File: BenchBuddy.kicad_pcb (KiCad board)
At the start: 4 copper layers, 165.1 x 63.5 mm, 133 parts, among them K1 1461069-5, P1 24 Pin MiniFit JR, P2 CONN_3X2, P3 CONN_2, P4 12 Pin Terminal Block, P5 3 Pin TB, Q1 2N3904, Q2 DMN65D8L-7, Q3 AOD476, Q4 AOD476, SW1 Power Switch, U1 LTV-816S, U11 LM317, U2 MCP3901, U3 LMT84, U4 OPA4170, U5 MCP4801, U6 LM337T, U7 AP5726, U8 LM337T, U9 LM317

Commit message: Layout Work Session 8 Output
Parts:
- R2, R5: moved to F.Cu
- moved R43 48.7 mm to (143.0, 99.8), turned to 90 degrees
- moved R1 16.1 mm to (159.3, 137.7), turned to 0 degrees
- moved R2 10.7 mm to (174.5, 126.0), turned to 0 degrees
- moved R26 7.13 mm to (120.1, 132.0)
- moved R27 7.13 mm to (122.7, 132.0)
- moved R28 7.13 mm to (125.1, 132.0)
- moved R29 7.13 mm to (128.0, 131.7)
- moved R31 6.35 mm to (135.5, 132.0)
- moved R30 6.35 mm to (132.6, 131.9)
- moved R32 6.35 mm to (137.9, 132.1)
- moved D1 5.99 mm to (172.2, 130.6), turned to 90 degrees
- moved R4 5.19 mm to (180.3, 137.9), turned to 0 degrees
- moved R3 5.06 mm to (178.8, 129.0), turned to 180 degrees
- moved R40 4.65 mm to (128.0, 94.5)
- moved R51 3.62 mm to (140.7, 94.5)
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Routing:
- net /Arduino/RELAY+: track 0.00 -> 54.5 mm
- net /Arduino/RELAY-: track 0.00 -> 44.3 mm
- net N-0000090: track 0.00 -> 20.1 mm
- net N-0000089: track 0.00 -> 19.2 mm
- net N-0000088: track 0.00 -> 13.9 mm, vias 0 -> 1
- net N-0000086: track 0.00 -> 13.7 mm
- net +12P: track 48.7 -> 62.0 mm, vias 2 -> 3
- net N-0000091: track 0.00 -> 8.35 mm
- net N-0000092: track 0.00 -> 5.56 mm, vias 0 -> 1
- net N-0000056: track 0.00 -> 5.18 mm
- net N-0000084: track 0.00 -> 4.38 mm
- net GND: track 30.6 -> 33.9 mm
- net GND_RELAY: track 1.65 -> 3.77 mm

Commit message: Layout Work Session 9 Output
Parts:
- moved C22 9.63 mm to (176.0, 90.4), turned to 270 degrees
- moved C17 7.56 mm to (178.1, 90.4), turned to 270 degrees
- moved D10 7.08 mm to (195.1, 90.7)
- moved C16 5.65 mm to (155.7, 89.9), turned to 270 degrees
- moved D8 5.50 mm to (174.5, 83.1), turned to 270 degrees
- moved D3 2.22 mm to (154.2, 83.1)
- moved R21 2.10 mm to (140.5, 78.7)
- moved C19 1.76 mm to (174.0, 90.4), turned to 270 degrees
- moved C20 1.67 mm to (196.6, 86.4)
- moved D9 1.67 mm to (185.9, 85.6)
- moved C18 1.65 mm to (159.8, 89.9), turned to 270 degrees
- moved C21 1.48 mm to (199.9, 85.6), turned to 0 degrees
- moved R53 0.90 mm to (203.7, 85.6)
- moved C23 0.86 mm to (157.7, 89.9), turned to 270 degrees
- moved D6 0.80 mm to (179.1, 82.8)
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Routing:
- net /PowerAdjustmentMonitor/V+_ADJ: track 0.00 -> 92.2 mm
- net /PowerAdjustmentMonitor/V-_ADJ: track 0.00 -> 89.7 mm
- net N-00000124: track 0.00 -> 57.0 mm
- net N-00000125: track 0.00 -> 48.0 mm
- net GND_PWR: track 0.00 -> 22.6 mm, vias 0 -> 1
- net +12V: track 209.0 -> 215.1 mm
- net +3.3V: track 145.5 -> 151.5 mm, vias 0 -> 1
- net -12V: track 212.4 -> 213.5 mm
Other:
- board text added: "ADD OUTPUT CAPACITANCE?"

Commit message: Layout Work Session 10 Output
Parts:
- C6: moved to F.Cu
- moved C6 38.4 mm to (208.0, 119.9), turned to 0 degrees
- moved C5 12.9 mm to (154.2, 120.7)
- moved R17 11.9 mm to (161.3, 115.6), turned to 180 degrees
- moved U7 10.5 mm to (159.3, 118.6), turned to 90 degrees
- moved C12 9.39 mm to (158.2, 108.7)
- moved L4 6.99 mm to (167.9, 120.7), turned to 90 degrees
- moved D5 6.80 mm to (172.2, 120.4), turned to 270 degrees
- moved JP4 0.57 mm to (89.7, 121.9)
- moved JP3 0.51 mm to (95.5, 117.3)
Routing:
- net +5P: track 10.5 -> 216.9 mm, vias 2 -> 3
- net /LED_Driver/LED_STRING+: track 0.00 -> 66.9 mm, vias 0 -> 2
- net /LED_Driver/LED_STRING-: track 0.00 -> 60.3 mm, vias 0 -> 2
- net N-00000120: track 0.00 -> 14.2 mm
- net GND_LED: track 2.83 -> 7.56 mm, vias 1 -> 4

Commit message: Layout Work Session 11 Output
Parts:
- added L5: INDUCTOR, SM0805, B.Cu at (165.2, 99.9)
- C6, R11: moved to B.Cu
- R16, R48, R49: moved to F.Cu
- moved C7 58.1 mm to (168.9, 99.9), turned to 180 degrees
- moved C1 53.0 mm to (167.5, 94.9), turned to 180 degrees
- moved C8 48.7 mm to (161.5, 99.9), turned to 180 degrees
- moved R16 37.3 mm to (174.4, 105.9)
- moved Q3 29.2 mm to (179.7, 103.8), turned to 180 degrees
- moved TH5 28.2 mm to (211.1, 112.4)
- moved C12 27.1 mm to (131.7, 114.3)
- moved R11 22.7 mm to (177.4, 104.9)
- moved R8 18.9 mm to (170.8, 97.4), turned to 0 degrees
- moved R9 17.0 mm to (178.1, 97.3), turned to 180 degrees
- moved D4 16.6 mm to (206.4, 104.0)
- moved R7 16.2 mm to (177.9, 100.2), turned to 0 degrees
- moved R48 16.1 mm to (157.2, 98.8)
- moved Q4 13.5 mm to (199.3, 103.6), turned to 180 degrees
- moved R15 13.4 mm to (173.9, 100.2)
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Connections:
- C2 pad 2: GND -> AGND
- C3 pad 2: GND -> AGND
- C4 pad 1: GND -> AGND
- C7 pad 2: +5V -> N-0000063
- JP1 pad 1: GND -> AGND
- JP2 pad 1: GND -> AGND
- JP3 pad 1: GND -> AGND
- JP4 pad 1: GND -> AGND
- P1 pad 3: GND -> AGND
- P1 pad 5: GND -> AGND
- P4 pad 6: /Thermocouple/TC IN - -> /Thermocouple/TC IN +
- P4 pad 7: /Thermocouple/TC IN + -> /Thermocouple/TC IN -
- R27 pad 2: GND -> AGND
- R28 pad 2: GND -> AGND
- R43 pad 2: GND -> AGND
- SW1 pad 3: GND -> AGND
- TP1 pad 1: GND -> AGND
- U2 pad 2: +5V -> N-0000063
- U4 pad 4: FE_V- -> FE_V+
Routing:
- net AGND: track 0.00 -> 157.9 mm, vias 0 -> 13
- net /Arduino/FAN_PWM: track 0.00 -> 72.9 mm, vias 0 -> 1
- net /Thermocouple/CH1+: track 0.00 -> 71.5 mm, vias 0 -> 1
- net /Thermocouple/TC IN +: track 0.00 -> 35.4 mm, vias 0 -> 1
- net GND: track 33.9 -> 0.00 mm, vias 1 -> 0
- net N-0000074: track 0.00 -> 32.3 mm, vias 0 -> 1
- net /Thermocouple/TC IN -: track 0.00 -> 31.7 mm
- net /Thermocouple/CH0+: track 0.00 -> 31.4 mm, vias 0 -> 1
- net N-0000077: track 0.00 -> 30.6 mm, vias 0 -> 1
- net FE_V-: track 0.00 -> 29.2 mm, vias 0 -> 1
- net FE_V+: track 0.00 -> 26.7 mm, vias 0 -> 2
- net +12C: track 187.2 -> 211.8 mm
- net N-0000069: track 0.00 -> 22.1 mm, vias 0 -> 1
- net N-0000064: track 0.00 -> 21.0 mm, vias 0 -> 2
- net /Arduino/CURR_MEAS: track 0.00 -> 20.9 mm
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
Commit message: Layout Work Session 12 Output
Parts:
- P3: footprint GND_POINT -> SM0805
- R24, R25, R35, R36, R38, R39, R41, R46: moved to B.Cu
- moved R14 60.3 mm to (78.3, 79.5), turned to 180 degrees
- moved R24 53.1 mm to (99.2, 83.8), turned to 180 degrees
- moved R23 51.5 mm to (99.2, 81.8), turned to 0 degrees
- moved R22 49.0 mm to (103.9, 81.7), turned to 0 degrees
- moved R25 46.0 mm to (104.0, 83.8), turned to 180 degrees
- moved C12 27.9 mm to (159.2, 109.3)
- moved R43 27.3 mm to (126.4, 121.5), turned to 180 degrees
- moved R41 12.6 mm to (130.7, 94.2)
- moved R28 7.05 mm to (125.5, 125.0)
- moved R27 6.97 mm to (122.6, 125.0)
- moved R33 6.87 mm to (140.4, 130.9)
- moved P3 6.25 mm to (155.3, 95.1), turned to 270 degrees
- moved R37 4.45 mm to (118.9, 95.6)
- moved R36 4.39 mm to (116.2, 94.6), turned to 90 degrees
- moved R34 3.86 mm to (111.3, 94.6)
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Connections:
- ARD1 pad 12: N-0000040 -> (no net)
- ARD1 pad 17: (no net) -> N-0000049
- C2 pad 2: AGND -> GND
- C3 pad 2: AGND -> GND
- C4 pad 1: AGND -> GND
- JP1 pad 1: AGND -> GND
- JP2 pad 1: AGND -> GND
- JP3 pad 1: AGND -> GND
- JP4 pad 1: AGND -> GND
- P1 pad 3: AGND -> GND
- P1 pad 5: AGND -> GND
- R27 pad 2: AGND -> GND
- R28 pad 2: AGND -> GND
- R41 pad 2: N-0000040 -> N-0000049
- R43 pad 2: AGND -> GND
- SW1 pad 3: AGND -> GND
- TP1 pad 1: AGND -> GND
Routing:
- net GND: track 0.00 -> 100.3 mm, vias 0 -> 4
- net /Fan/TACH_IN: track 0.00 -> 93.5 mm
- net /Arduino/MOSI: track 0.00 -> 71.7 mm, vias 0 -> 1
- net /Arduino/SCLK: track 0.00 -> 70.0 mm, vias 0 -> 2
- net /Arduino/V+_ADJ_MON: track 0.00 -> 67.7 mm, vias 0 -> 1
- net /Arduino/V-_ADJ_MON: track 0.00 -> 64.9 mm, vias 0 -> 1
- net N-00000114: track 0.00 -> 64.0 mm
- net /Arduino/MISO: track 0.00 -> 59.2 mm, vias 0 -> 1
- net /Arduino/CURR_MEAS: track 20.9 -> 75.5 mm
- net /PowerAdjustmentMonitor/V-_ADJ: track 89.7 -> 144.2 mm
- net /Arduino/LED_EN_PWM: track 0.00 -> 53.7 mm, vias 0 -> 1
- net /PowerAdjustmentMonitor/V+_ADJ: track 92.2 -> 142.1 mm, vias 0 -> 1
- net /Arduino/~RESET: track 0.00 -> 47.5 mm, vias 0 -> 1
- net /Arduino/~ADC_CS: track 0.00 -> 45.5 mm, vias 0 -> 1
- net /Arduino/FAN_MODE: track 0.00 -> 43.4 mm, vias 0 -> 2
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
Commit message: Layout Work Session 14 Output
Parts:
- removed R26: R, SM0805-blob
- added C26: C, SM1210, B.Cu at (212.4, 92.2)
- added C27: C, SM1210, B.Cu at (211.5, 87.3)
- added C28: C, SM1210, B.Cu at (211.6, 83.8)
- added C29: C, SM1210, B.Cu at (211.7, 79.8)
- added C30: C, SM0805, B.Cu at (162.9, 104.4)
- added C31: C, SM0805, F.Cu at (158.2, 94.2)
- added R56: R, SM0805, F.Cu at (210.0, 91.5)
- R27, R28, R29, R30, R31, R32, R33, R34, R35, R36, R37, R38, R39, R40, R41, R42, R46, R47, R50, R51: footprint SM0805-blob -> SM0805-SB
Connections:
- U2 pad 10: (no net) -> AGND
- U2 pad 15: (no net) -> N-0000064
- U2 pad 16: (no net) -> N-0000065
- U2 pad 9: (no net) -> N-0000070
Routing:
- net N-0000095: track 4.78 -> 51.2 mm
- net /Fan/TACH_IN: track 93.5 -> 117.8 mm
- net AGND: track 130.2 -> 150.8 mm
- net GND_PWR: track 26.7 -> 47.2 mm
- net N-0000099: track 50.3 -> 66.8 mm
- net +5V: track 19.5 -> 32.9 mm
- net N-0000087: track 0.00 -> 5.20 mm
- net /PowerAdjustmentMonitor/V+_ADJ: track 142.1 -> 146.3 mm
- net +5P: track 212.7 -> 216.6 mm
- net N-0000074: track 32.3 -> 28.3 mm
- net N-00000124: track 7.45 -> 11.1 mm
- net N-0000065: track 0.00 -> 3.27 mm, vias 0 -> 1
- net N-0000070: track 0.00 -> 3.21 mm
- net N-0000064: track 0.00 -> 3.12 mm, vias 0 -> 1
- net +12V: track 220.8 -> 223.9 mm
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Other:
- net class Default: clearance 0.254 -> 0.1524
- rule pad_to_mask_clearance: 0.254 -> 0
- rule trace_clearance: 0.254 -> 0.1524
- board text removed: "ADD OUTPUT CAPACITANCE?"
- board text removed: "Do we need a second GND?"

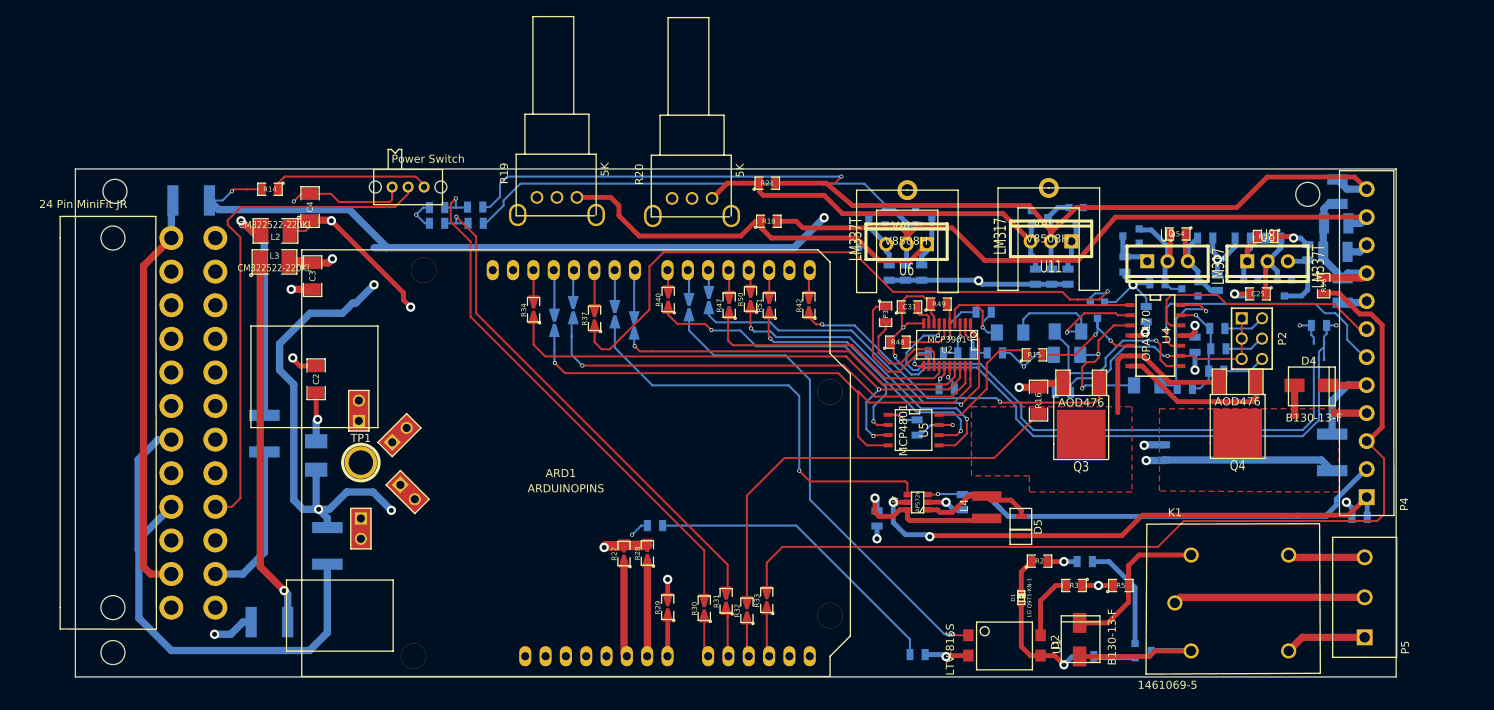
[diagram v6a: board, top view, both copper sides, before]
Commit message: Layout Work Session 15 Output
Silkscreen
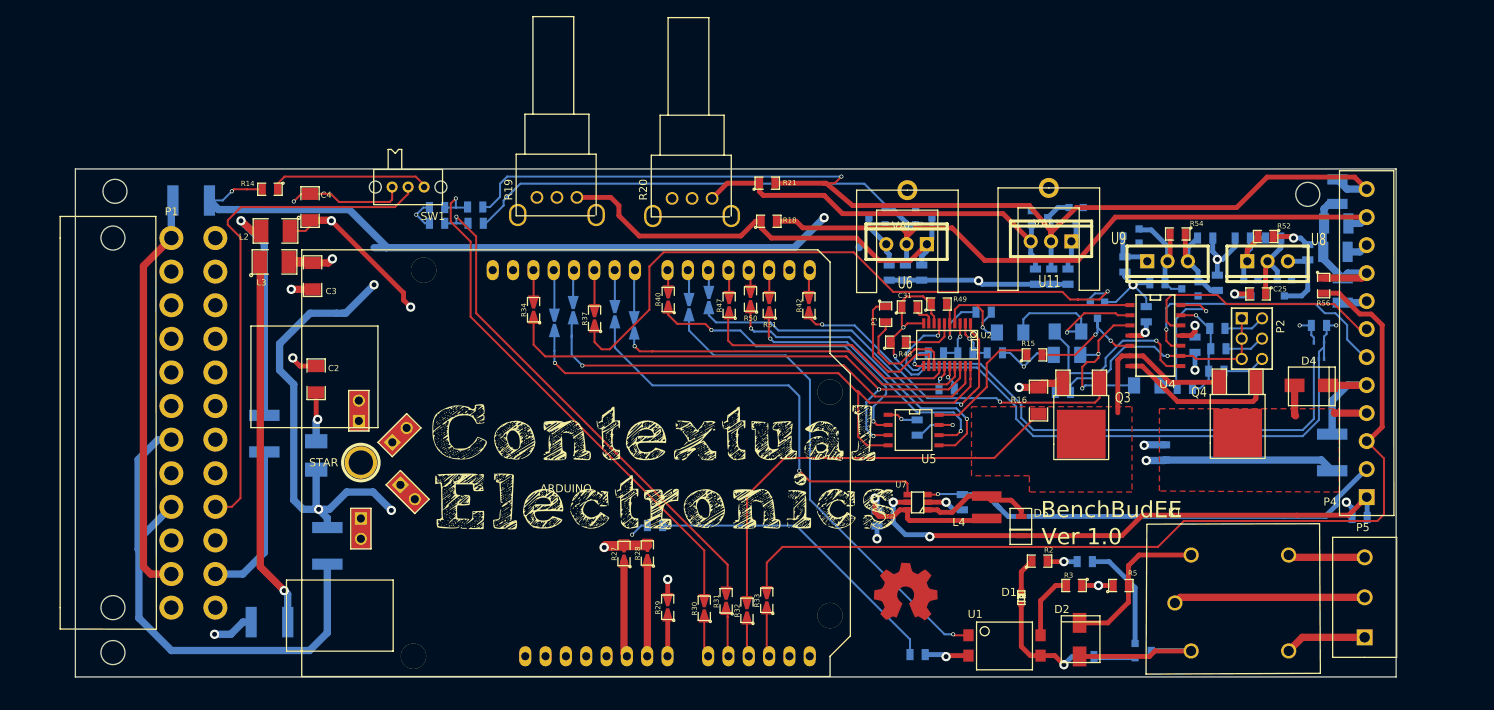
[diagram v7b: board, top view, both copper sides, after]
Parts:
- added G***: CE-LOGO, CE-LOGO, F.Cu at (127.2, 114.1)
- added G***: OSHW_CU, OSHW_CU, B.SilkS at (157.9, 129.9)
- added G***: OSHW_SM, OSHW_SM, B.SilkS at (157.9, 129.9)
- ARD1: value ARDUINOPINS -> ARDUINO
- renumbered TP1 to STAR
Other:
- board text added: "BenchBudEE"
- board text added: "For more information, visit: https://GitHub.com/ContextualElectronics/BenchBudEE or http://ContextualElectronics.com"
- board text added: "Ver 1.0"

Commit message: Layout Work Session 16
Added ground connect to heatsink, fixed relay trace width, fixed silk
screen issues.
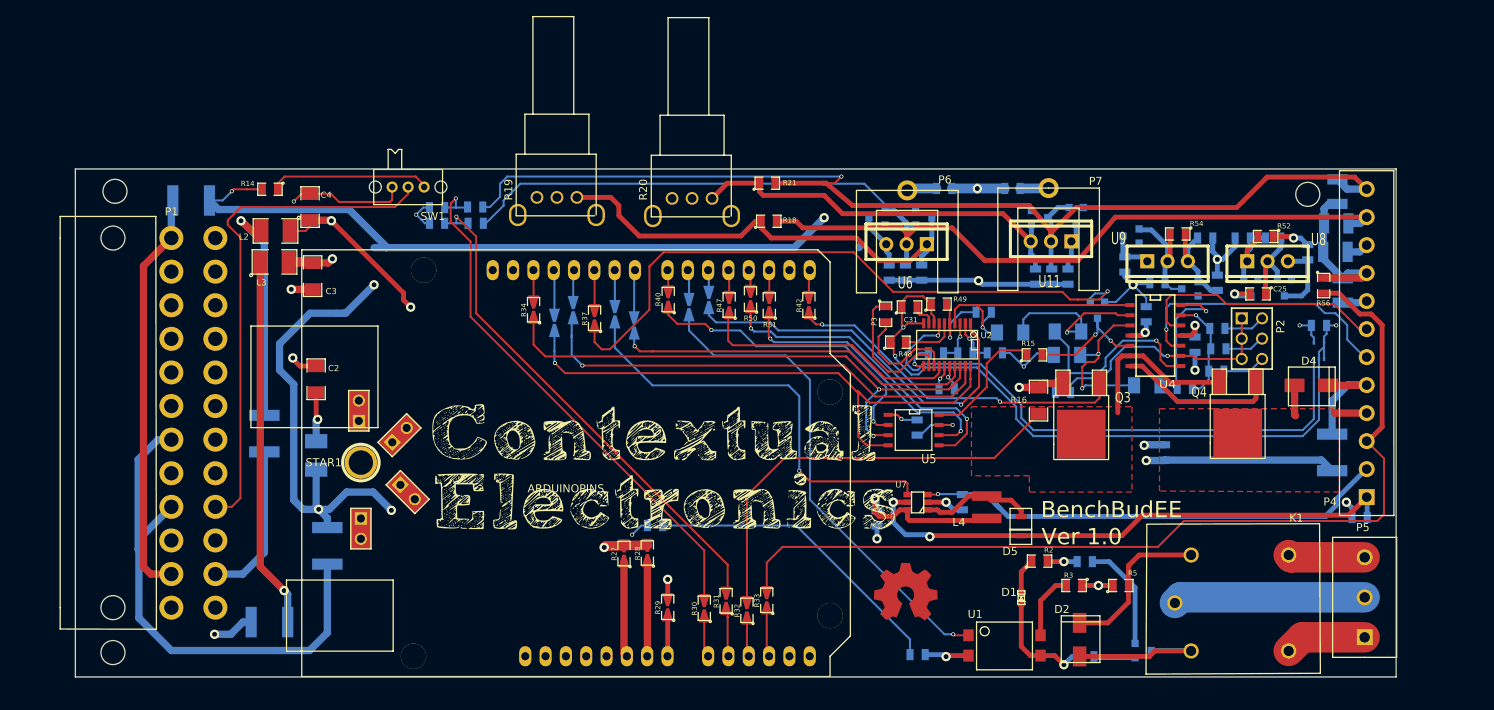
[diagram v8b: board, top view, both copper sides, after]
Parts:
- removed STAR: CONN_1, 1pin
- removed V8508H (x2): VAL**, V8508H
- added P6: CONN_1, V8508H, F.Cu at (158.0, 79.6)
- added P7: CONN_1, V8508H, F.Cu at (175.6, 79.3)
- added R26: R, SM0805, B.Cu at (162.6, 79.4)
- added R57: R, SM0805, B.Cu at (171.1, 79.4)
- added STAR1: CONN_1, 1pin, F.Cu at (89.7, 113.7)
- ARD1: value ARDUINO -> ARDUINOPINS
- D1: footprint LED-0603 -> LED-0603-2
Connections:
- ARD1 pad 1: N-0000038 (its old number) -> (no net)
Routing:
- net GND_PWR: track 47.2 -> 53.9 mm, vias 2 -> 3
- net N-00000128: track 0.00 -> 3.76 mm
- net N-00000127: track 0.00 -> 3.59 mm
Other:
- net class AC added: clearance 1.524, trace_width 3.81, via_dia 1.1684, via_drill 0.6096
